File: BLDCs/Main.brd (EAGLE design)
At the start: 160 x 100 mm, 51 parts, among them IC1 MEGA8-AI, IC2 LM1117DTX-5.0, J1 PIC_ICSP_MINI_5_PIN, J4 SPI, U4 LM1117 3.3, Y1 16MHZ

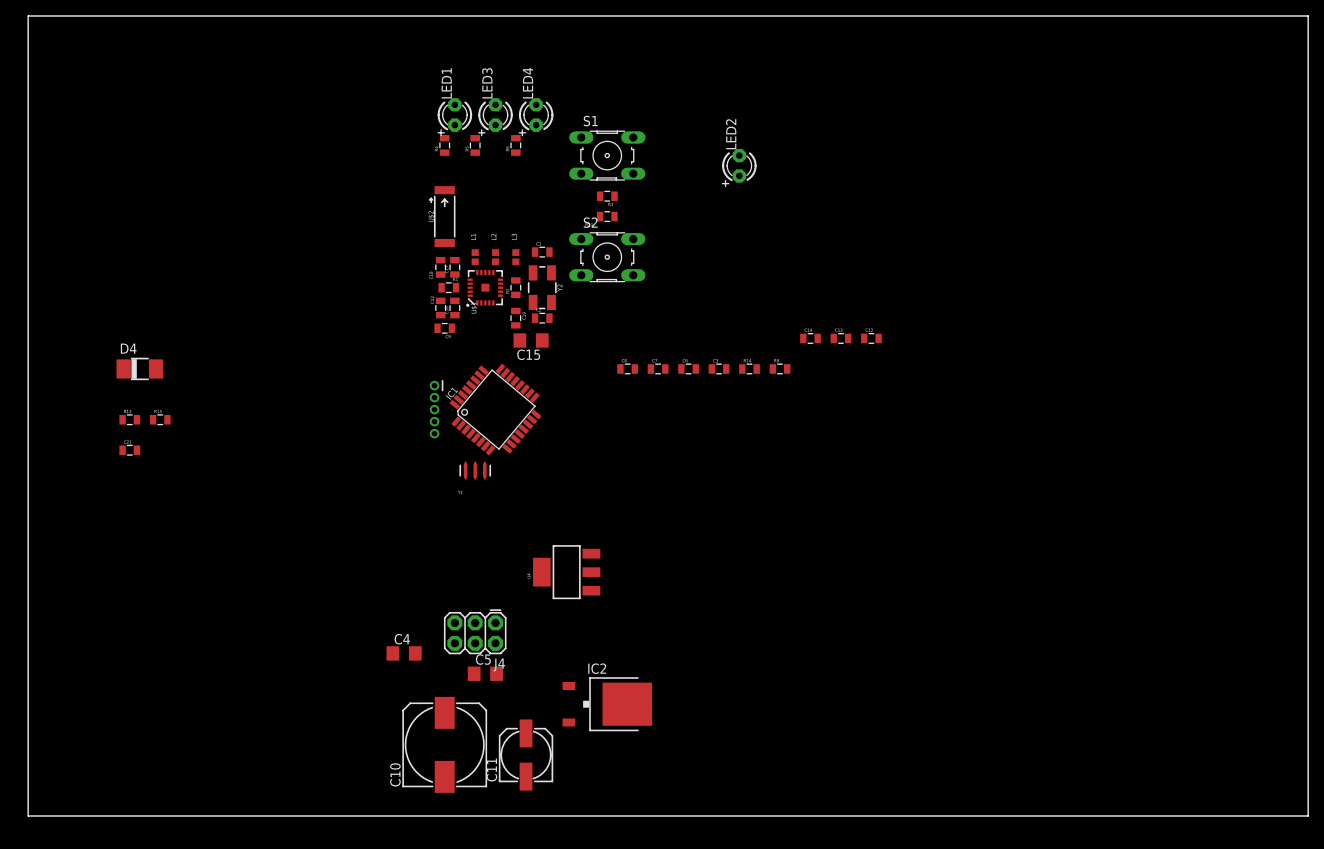
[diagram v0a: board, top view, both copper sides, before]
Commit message: add license
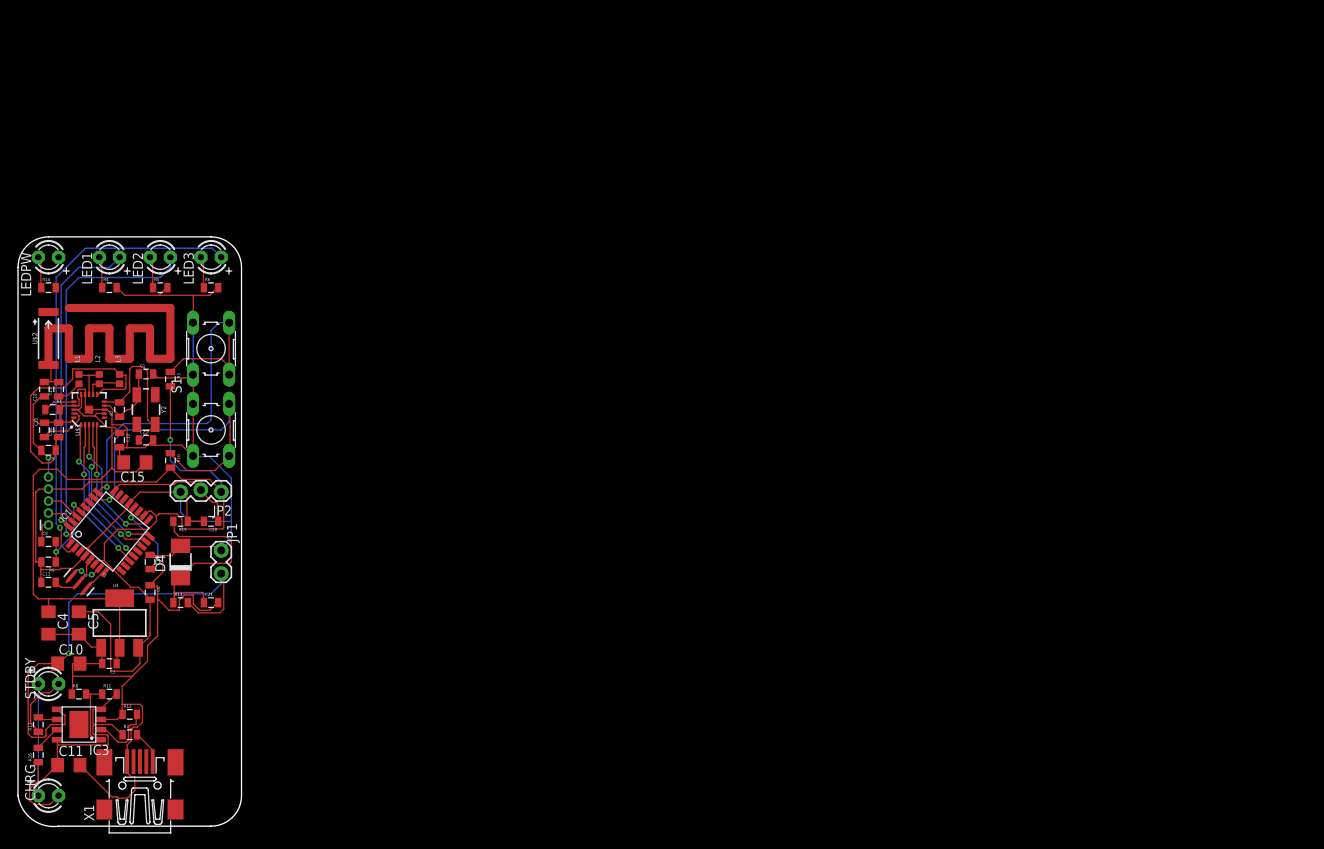
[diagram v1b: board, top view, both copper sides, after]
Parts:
- removed C12, C14: 0.1uF, SparkFun-Passives:0805
- removed IC2: LM1117DTX-5.0, lm1117:TO252
- removed J4: SPI, SparkFun-Connectors:2X3
- removed LED4: PW, adafruit:LED3MM
- added C20: 22p, SparkFun-Passives:0805
- added CHRG, LEDPW, STDBY: PW, adafruit:LED3MM
- added IC3: TP4056, TP4056:SOP-8
- added JP1: (no value), SparkFun:1X02_LOCK
- added JP2: (no value), SparkFun:1X03_LOCK
- added R11, R12, R7, R8: 2.2k, SparkFun-Resistors:0805
- added R16, R17: 102, SparkFun-Resistors:0805
- added X1: MINI-USB-32005-201, con-cypressindustries:32005-201
- C10: value 220/50 -> 10uF; device adafruit:153CLV-1010 -> adafruit:C1206
- C11: value 100/35 -> 10uF; device adafruit:153CLV-0605 -> adafruit:C1206
- R4, R5, R6: value 1k -> 330
- moved C13 103.6 mm to (2.54, 29.2)
- moved R9 94.6 mm to (2.54, 31.8), turned to 180 degrees
- moved R14 88.2 mm to (2.54, 66.0)
- moved C3 84.6 mm to (10.2, 19.1), turned to 180 degrees
- moved C8 75.5 mm to (2.54, 34.3)
- moved LED2 73.3 mm to (16.5, 69.8), turned to 180 degrees
- moved C6 72.9 mm to (15.2, 27.9), turned to 270 degrees
- moved C7 67.9 mm to (15.2, 31.8), turned to 270 degrees
- moved R10 62.5 mm to (17.8, 44.5), turned to 270 degrees
- moved R3 59.2 mm to (17.8, 54.6), turned to 270 degrees
- moved C11 57.2 mm to (5.08, 6.35), turned to 0 degrees
- moved U4 56.2 mm to (11.4, 24.1), turned to 0 degrees
- moved S1 55.1 mm to (22.9, 58.4), turned to 90 degrees
- moved S2 54.0 mm to (22.9, 48.3), turned to 90 degrees
- moved C1 51.8 mm to (14.7, 55.2)
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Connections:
- removed net 12V: C10.+, C12.1, IC2.2
- new net N$11: IC1.23
- new net N$13: IC3.7, R16.2
- new net N$22: IC3.6, R17.2
- new net N$23: R17.1, STDBY.K
- new net N$24: CHRG.K, R16.1
- new net N$25: C11.1, CHRG.A, IC3.4, IC3.8, R11.2, R7.1, STDBY.A
- new net N$27: IC3.2, R12.2
- new net N$29: IC3.1, R11.1, R8.2
- new net N$30: R7.2, X1.5
- net 3.3V: now also C15.1, C19.1, U$1.15, U$1.18, U$1.7
- net A0: no longer IC1.23
- net A1: now also C20.1, JP2.2
- net BATT_IN: now also C10.1, IC3.5, JP1.1
- net D3: now also LED2.A; no longer LED3.A
- net D4: now also LED3.A; no longer LED4.A
- net GND: now also C10.2, C11.2, C20.2, IC3.3, JP1.2, JP2.3, R12.1, R8.1, X1.1; no longer C10.-, C11.-, C12.2, C14.2, IC2.1, J4.6, R14.2
- net MISO: no longer J4.1
- net MOSI: no longer J4.4
- net N$12: now also LEDPW.K; no longer LED2.K
- net N$2: now also LED2.K; no longer LED3.K
- net N$3: now also LED3.K; no longer LED4.K
- net RST: no longer J4.5
- net SCK: no longer J4.3
- net VCC: now also JP2.1; no longer C11.+, C14.1, C15.1, C19.1, IC2.TAB, J4.2, LED2.A, U$1.15, U$1.18, U$1.7
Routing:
- net GND: track 0.00 -> 242.8 mm, vias 0 -> 1
- net VCC: track 0.00 -> 122.1 mm, vias 0 -> 1
- net 3.3V: track 0.00 -> 67.9 mm
- net N$19: track 0.00 -> 62.0 mm
- net BATT_IN: track 0.00 -> 59.6 mm, vias 0 -> 1
- net D4: track 0.00 -> 58.7 mm, vias 0 -> 1
- net A2: track 0.00 -> 51.3 mm, vias 0 -> 1
- net D3: track 0.00 -> 47.6 mm, vias 0 -> 1
- net A3: track 0.00 -> 43.1 mm, vias 0 -> 1
- net N$25: track 0.00 -> 43.0 mm
- net D2: track 0.00 -> 39.4 mm, vias 0 -> 1
- net N$16: track 0.00 -> 33.9 mm
- net A0: track 0.00 -> 27.8 mm
- net D7: track 0.00 -> 19.5 mm, vias 0 -> 2
- net D8: track 0.00 -> 19.5 mm, vias 0 -> 2
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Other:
- board size 160 x 100 mm -> 27.9 x 73.7 mm

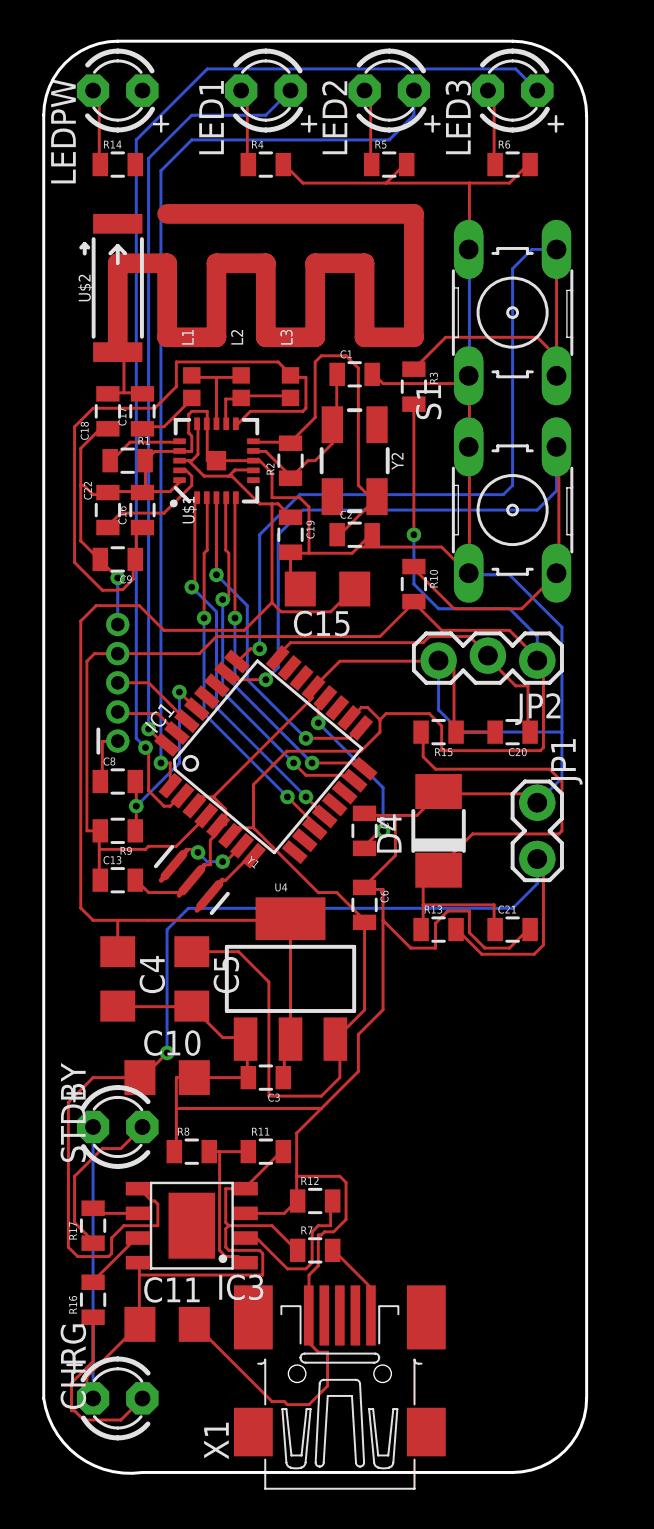
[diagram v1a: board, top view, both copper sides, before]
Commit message: add license
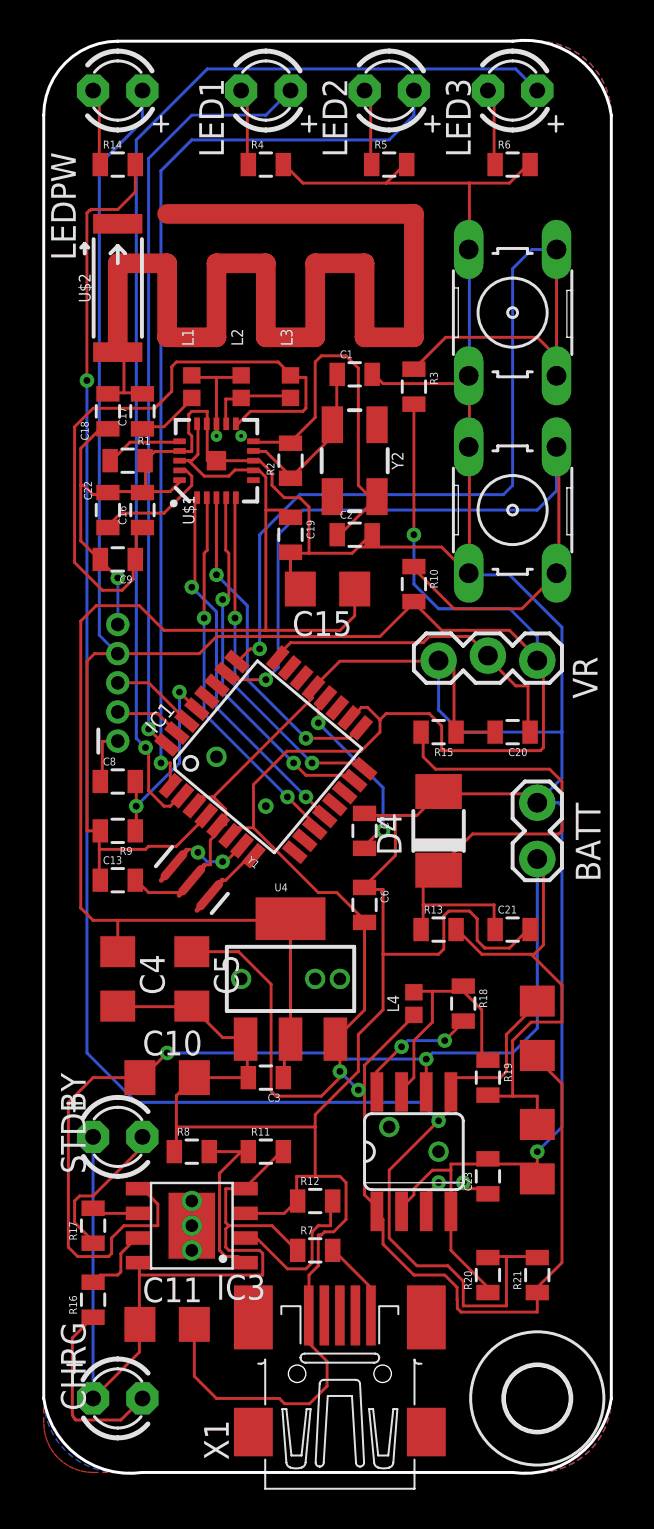
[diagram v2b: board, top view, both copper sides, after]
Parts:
- added C12: 0.1mF, adafruit:C1206
- added C14: 0.22mF, adafruit:C1206
- added C23: 1.5nF, SparkFun-Passives:0805
- added H1: MOUNT-HOLE3.3, holes:3,3
- added L4: 100uH, SparkFun-Coils:0402
- added R18: 180, SparkFun-Resistors:0805
- added R19: 0.22, SparkFun-Resistors:0805
- added R20: 2.2K, SparkFun-Resistors:0805
- added R21: 6.8K, SparkFun-Resistors:0805
- added U$3: MC33063/MC34063D, adafruit:SO08
- moved STDBY 0.51 mm to (2.54, 16.0)
- renumbered JP1 to BATT, JP2 to VR
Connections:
- new net N$26: C14.2, R14.2, R20.2, R21.2, U$3.5
- new net N$28: C23.1, U$3.3
- new net N$34: R18.2, U$3.8
- new net N$35: L4.2, R18.1, R19.1, U$3.7
- net BATT_IN: now also C12.1, R19.2, U$3.6
- net GND: now also C12.2, C23.2, R20.1, U$3.2, U$3.4
- net VCC: now also C14.1, L4.1, LEDPW.A, R21.1, U$3.1
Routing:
- net N$26: track 0.00 -> 97.4 mm, vias 0 -> 2
- net VCC: track 122.1 -> 191.4 mm, vias 1 -> 3
- net GND: track 242.8 -> 279.3 mm, vias 1 -> 2
- net BATT_IN: track 59.6 -> 76.2 mm, vias 1 -> 2
- net N$35: track 0.00 -> 12.8 mm
- net N$34: track 0.00 -> 6.60 mm, vias 0 -> 2
- net N$28: track 0.00 -> 4.87 mm, vias 0 -> 2
- net 3.3V: track 67.9 -> 69.4 mm
- net N$20: track 9.66 -> 10.9 mm
- net N$25: track 43.0 -> 42.0 mm
- net N$23: track 8.38 -> 7.72 mm
- net N$13: track 3.30 -> 3.83 mm
- added copper zone on layer 16, net B
- added copper zone on layer 1, net T
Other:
- board size 27.9 x 73.7 mm -> 29.2 x 73.7 mm

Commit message: add new nfr
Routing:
- net VCC: track 191.4 -> 192.3 mm
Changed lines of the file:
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@@
 <drawing>
 <settings>
-<setting alwaysvectorfont="yes"/>
+<setting alwaysvectorfont="no"/>
 <setting verticaltext="up"/>
 </settings>
@@
 <attribute name="NAME" x="17.018" y="22.86" size="0.6096" layer="25" font="vector" ratio="20" rot="R90" align="bottom-center"/>
 <attribute name="PROD_ID" value="NDUC-13457" x="17.78" y="22.86" size="1.778" layer="27" rot="R90" display="off"/>
-<attribute name="VALUE" x="19.812" y="22.86" size="0.6096" layer="27" font="vector" ratio="20" rot="R90" align="top-center"/>
+<attribute name="VALUE" x="17.78" y="24.892" size="0.6096" layer="27" font="vector" ratio="20" rot="R180" align="top-center"/>
 </element>
 <element name="R18" library="SparkFun-Resistors" package="0805" value="180" x="20.32" y="22.86" smashed="yes" rot="R270">
@@
 <wire x1="3.4925" y1="29.21" x2="3.44" y2="29.21" width="0.1524" layer="1"/>
 <wire x1="5.715" y1="28.575" x2="6.35" y2="29.21" width="0.1524" layer="1"/>
-<wire x1="7.62" y1="31.59125" x2="7.62" y2="31.90875" width="0.1524" layer="1"/>
-<wire x1="7.3025" y1="31.27375" x2="7.62" y2="31.59125" width="0.1524" layer="1"/>
-<wire x1="7.3025" y1="30.00375" x2="7.3025" y2="31.27375" width="0.1524" layer="1"/>
-<wire x1="6.985" y1="30.00375" x2="7.3025" y2="30.00375" width="0.1524" layer="1"/>
+<wire x1="7.62" y1="31.456384375" x2="7.62" y2="31.90875" width="0.1524" layer="1"/>
 <wire x1="7.62" y1="31.90875" x2="7.7071875" y2="32.0145625" width="0.1524" layer="1"/>
-<wire x1="6.985" y1="30.00375" x2="6.35" y2="29.21" width="0.1524" layer="1"/>
+<wire x1="6.985" y1="30.00375" x2="6.9695125" y2="29.984390625" width="0.1524" layer="1"/>
+<wire x1="6.9695125" y1="29.984390625" x2="6.35" y2="29.21" width="0.1524" layer="1"/>
 <wire x1="6.82625" y1="33.49625" x2="6.50875" y2="33.17875" width="0.1524" layer="1"/>
 <wire x1="7.46125" y1="33.49625" x2="6.82625" y2="33.49625" width="0.1524" layer="1"/>
 <wire x1="8.09625" y1="32.86125" x2="7.46125" y2="33.49625" width="0.1524" layer="1"/>
-<wire x1="8.09625" y1="32.0675" x2="8.09625" y2="32.86125" width="0.1524" layer="1"/>
-<wire x1="7.77875" y1="32.0675" x2="8.09625" y2="32.0675" width="0.1524" layer="1"/>
 <wire x1="6.50875" y1="33.17875" x2="6.481515625" y2="33.043021875" width="0.1524" layer="1"/>
 <wire x1="7.77875" y1="32.0675" x2="7.7071875" y2="32.0145625" width="0.1524" layer="1"/>
@@
 <wire x1="20.6375" y1="27.6225" x2="21.034375" y2="27.225625" width="0.1524" layer="1"/>
 <wire x1="21.034375" y1="27.225625" x2="21.034375" y2="26.114375" width="0.1524" layer="1"/>
+<wire x1="7.3307" y1="30.345578125" x2="6.9695125" y2="29.984390625" width="0.1524" layer="1"/>
+<wire x1="7.62" y1="31.456384375" x2="7.3307" y2="31.167084375" width="0.1524" layer="1"/>
+<wire x1="7.3307" y1="31.167084375" x2="7.3307" y2="30.345578125" width="0.1524" layer="1"/>
+<wire x1="7.7071875" y1="32.0145625" x2="8.09625" y2="32.403625" width="0.1524" layer="1"/>
+<wire x1="8.09625" y1="32.403625" x2="8.09625" y2="32.86125" width="0.1524" layer="1"/>
 </signal>
 <signal name="VCC">
@@
 <wire x1="13.81125" y1="21.11375" x2="13.7414" y2="21.0312" width="0.1524" layer="1"/>
 <wire x1="8.73125" y1="31.90875" x2="8.41375" y2="31.59125" width="0.1524" layer="1"/>
-<wire x1="9.525" y1="31.90875" x2="8.73125" y2="31.90875" width="0.1524" layer="1"/>
-<wire x1="12.85875" y1="28.575" x2="9.525" y2="31.90875" width="0.1524" layer="1"/>
+<wire x1="12.85875" y1="28.575" x2="9.921875" y2="31.511875" width="0.1524" layer="1"/>
+<wire x1="9.921875" y1="31.511875" x2="9.525" y2="31.90875" width="0.1524" layer="1"/>
 <wire x1="13.81125" y1="28.575" x2="12.85875" y2="28.575" width="0.1524" layer="1"/>
 <wire x1="15.24" y1="27.14625" x2="13.81125" y2="28.575" width="0.1524" layer="1"/>
@@
 <wire x1="16.03375" y1="37.465" x2="15.39875" y2="38.1" width="0.1524" layer="1"/>
 <wire x1="16.03375" y1="36.83" x2="16.03375" y2="37.465" width="0.1524" layer="1"/>
-<wire x1="9.525" y1="31.90875" x2="9.525" y2="34.13125" width="0.1524" layer="1"/>
+<wire x1="9.525" y1="31.90875" x2="9.525" y2="32.705309375" width="0.1524" layer="1"/>
 <wire x1="14.605" y1="37.62375" x2="14.45131875" y2="37.562746875" width="0.1524" layer="1"/>
 <wire x1="1.5875" y1="31.75" x2="1.5875" y2="30.7975" width="0.1524" layer="1"/>
@@
 <wire x1="24.13" y1="6.985" x2="20.20644375" y2="6.985" width="0.1524" layer="1"/>
 <wire x1="24.13" y1="7.99" x2="24.13" y2="6.985" width="0.1524" layer="1"/>
+<wire x1="8.320021875" y1="31.50033125" x2="8.729846875" y2="31.91015625" width="0.1524" layer="1"/>
+<wire x1="8.729846875" y1="31.91015625" x2="9.525" y2="32.705309375" width="0.1524" layer="1"/>
+<wire x1="9.525" y1="32.705309375" x2="9.525" y2="34.13125" width="0.1524" layer="1"/>
+<wire x1="9.52359375" y1="31.91015625" x2="9.525" y2="31.90875" width="0.1524" layer="1"/>
 </signal>
 <signal name="3.3V">
@@
 <wire x1="17.145" y1="18.415" x2="17.145" y2="18.3134" width="0.1524" layer="1"/>
 </signal>
-<signal name="N$31">
-<via x="6.35" y="12.7" extent="1-16" drill="0.65"/>
-</signal>
-<signal name="N$32">
-<via x="6.35" y="11.43" extent="1-16" drill="0.65"/>
-</signal>
-<signal name="N$33">
-<via x="6.35" y="10.16" extent="1-16" drill="0.65"/>
-</signal>
 <signal name="N$36">
 <via x="16.51" y="16.51" extent="1-16" drill="0.65"/>
@@
 <via x="10.16" y="33.02" extent="1-16" drill="0.4"/>
 </signal>
-<signal name="N$43">
-<via x="7.62" y="52.07" extent="1-16" drill="0.2"/>
-</signal>
-<signal name="N$44">
-<via x="8.89" y="52.07" extent="1-16" drill="0.2"/>
-</signal>
 <signal name="B">
